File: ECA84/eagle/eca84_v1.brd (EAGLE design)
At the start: 223 x 127 mm, 34 parts

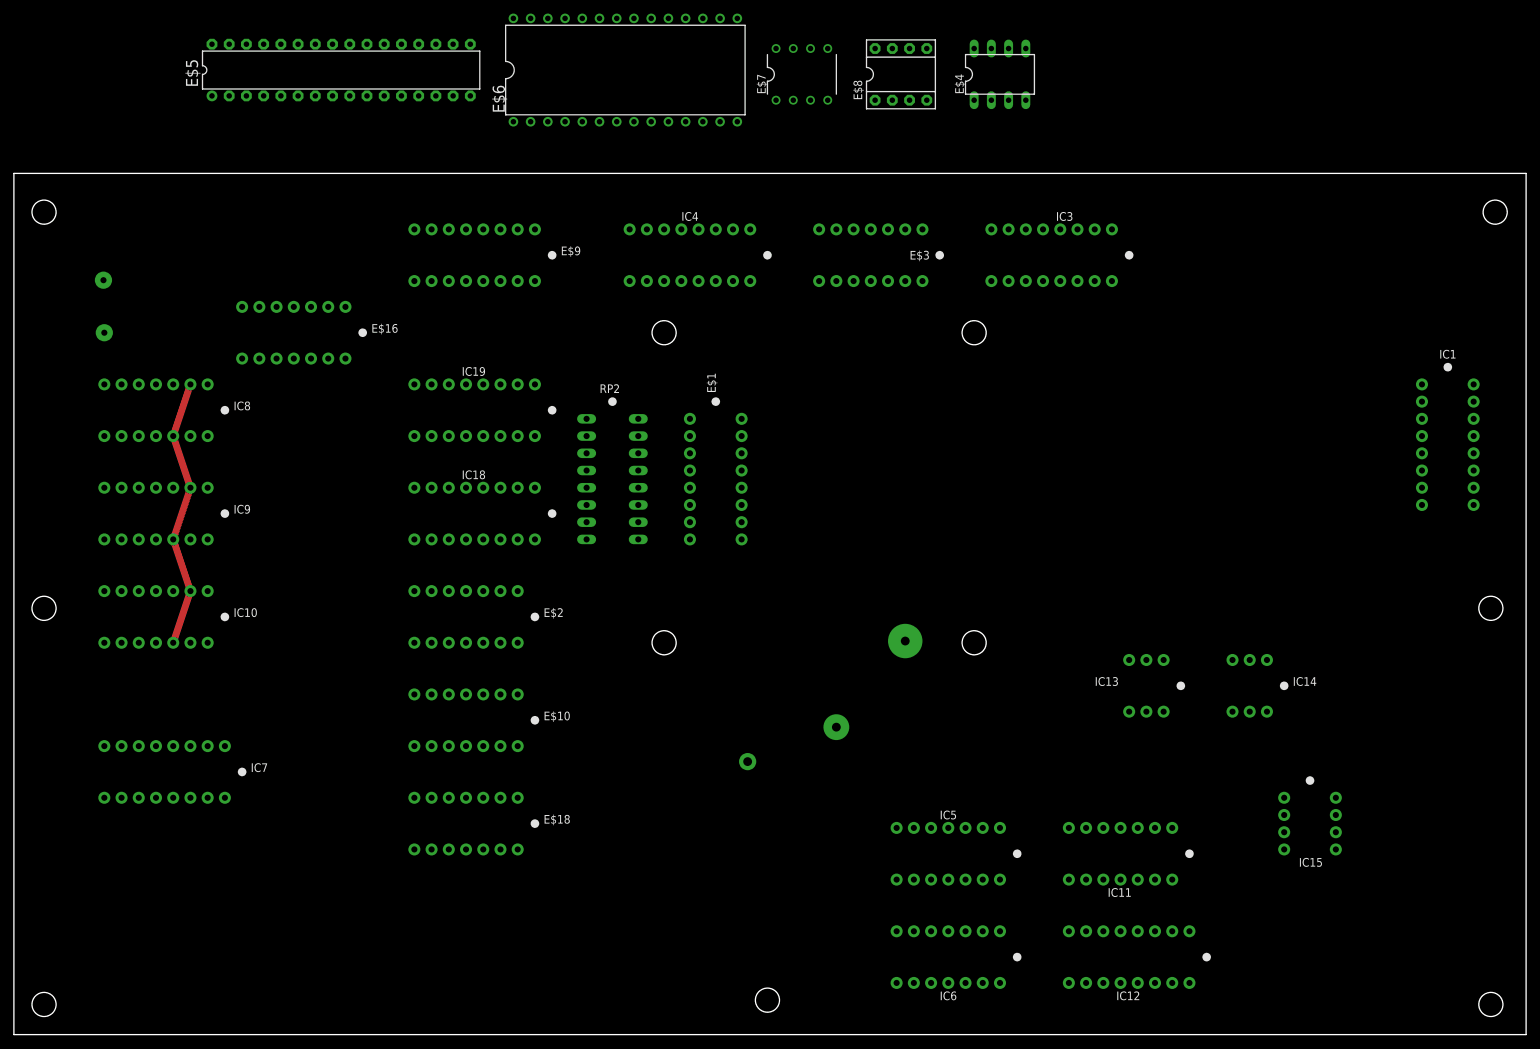
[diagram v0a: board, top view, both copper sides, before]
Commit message: trazado top, agr poligono vcc
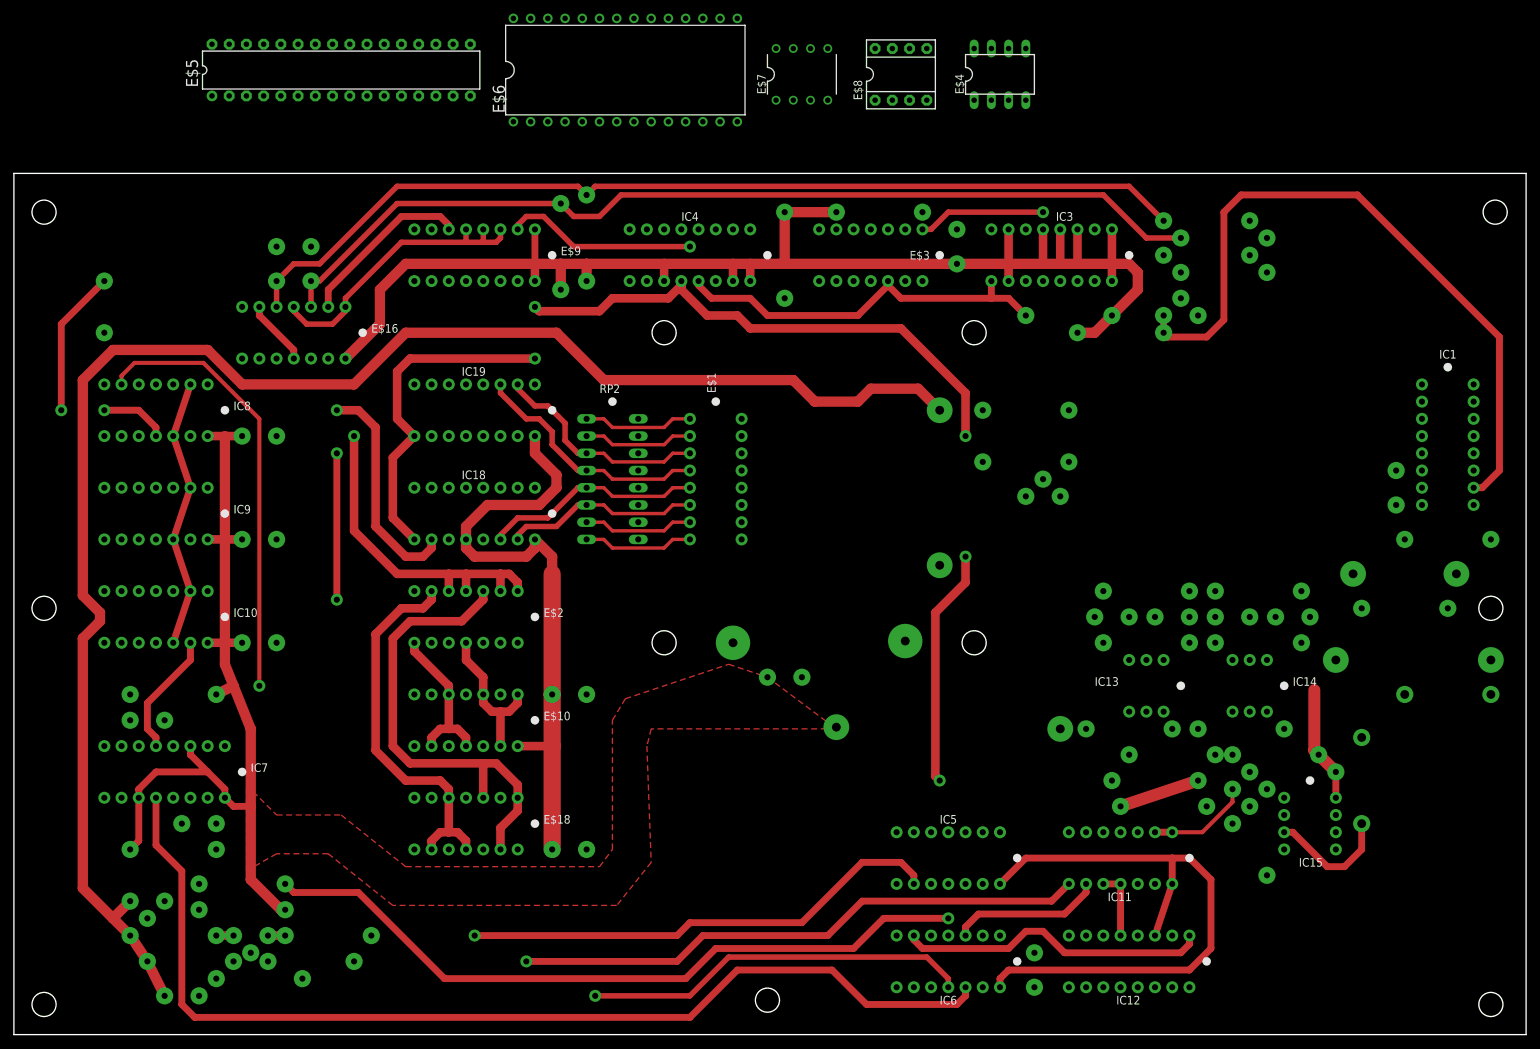
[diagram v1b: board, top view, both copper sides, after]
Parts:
- removed E$13: (no value), eca84:ROUND-4
- added E$100, E$101, E$102, E$103, E$104, E$105, E$106, E$107, E$108, E$109, E$110, E$111, E$112, E$113, E$114, E$115, E$116, E$117, E$118, E$119, E$120, E$121, E$122, E$123, E$124, E$125, E$126, E$127, E$128, E$129, E$130, E$131, E$132, E$133, E$134, E$135, E$136, E$137, E$138, E$139, E$140, E$141, E$142, E$143, E$147, E$148, E$152, E$153, E$154, E$168, E$20, E$21, E$22, E$23, E$24, E$25, E$26, E$27, E$28, E$29, E$30, E$31, E$32, E$33, E$34, E$35, E$36, E$37, E$38, E$39, E$40, E$41, E$42, E$43, E$44, E$45, E$46, E$47, E$48, E$49, E$50, E$51, E$52, E$53, E$54, E$55, E$62, E$63, E$64, E$65, E$66, E$67, E$68, E$69, E$70, E$71, E$72, E$73, E$74, E$75, E$76, E$77, E$78, E$79, E$80, E$81, E$82, E$83, E$84, E$85, E$86, E$87, E$88, E$89, E$90, E$91, E$92, E$93, E$94, E$95, E$96: (no value), eca84:ROUND-3
- added E$144, E$159, E$160, E$161, E$162, E$163, E$166: (no value), eca84:ROUND-5
- added E$145, E$146, E$149, E$150, E$151, E$164, E$165, E$17, E$19, E$56, E$57, E$58, E$59, E$60, E$61, E$97, E$98, E$99: (no value), eca84:ROUND-1
- added E$155, E$156, E$157, E$158: (no value), eca84:ROUND-4
- added E$167: (no value), eca84:ROUND-6
- moved IC11 0.64 mm to (163.2, 26.0)
- moved IC5 0.64 mm to (137.8, 26.0)
- moved IC12 0.63 mm to (164.5, 10.8)
- moved IC6 0.63 mm to (137.8, 10.8)
- moved E$11 0.18 mm to (13.3, 111.1)
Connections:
- new net S$10: IC6.P$12, IC7.P$12
- new net S$11: E$42.P$1, E$43.P$1
- new net S$12: E$47.P$1, E$48.P$1
- new net S$13: E$144.P$1, E$34.P$1, E$37.P$1, E$38.P$1, E$39.P$1
- new net S$14: E$56.P$1, E$57.P$1
- new net S$15: E$16.P$5, E$62.P$1, E$67.P$1, E$72.P$1
- new net S$16: E$16.P$3, E$63.P$1, E$66.P$1, E$73.P$1
- new net S$17: E$16.P$2, E$9.P$6
- new net S$18: E$16.P$1, E$16.P$4, E$9.P$3, E$9.P$4, E$9.P$5
- new net S$19: E$149.P$1, E$9.P$2
- new net S$2: E$11.P$1, E$19.P$1
- new net S$20: E$16.P$14, E$68.P$1, E$69.P$1, E$80.P$1, E$81.P$1, E$83.P$1, E$9.P$1, E$9.P$16, E$95.P$1, E$96.P$1, IC3.P$1, IC3.P$10, IC3.P$16, IC3.P$3, IC3.P$4, IC3.P$5, IC3.P$7, IC4.P$11, IC4.P$15, IC4.P$16
- new net S$21: E$150.P$1, E$61.P$1, IC4.P$12
- new net S$22: E$2.P$1, E$2.P$2, E$2.P$4, E$2.P$5, E$59.P$1
- new net S$23: E$3.P$12, E$82.P$1, IC3.P$9, IC4.P$13
- new net S$24: E$58.P$1, IC18.P$10
- new net S$25: E$60.P$1, IC18.P$9, IC19.P$9
- new net S$26: E$1.P$3, IC19.P$2, RP2.P$3
- new net S$27: E$1.P$4, IC19.P$3, RP2.P$4
- new net S$28: E$1.P$6, IC18.P$15, RP2.P$6
- new net S$29: E$1.P$7, RP2.P$7
- new net S$3: E$17.P$1, IC8.P$11
- new net S$30: E$10.P$14, E$91.P$1, E$93.P$1, IC18.P$12, IC18.P$16, IC19.P$16
- new net S$31: E$1.P$1, RP2.P$1
- new net S$32: E$1.P$2, RP2.P$2
- new net S$33: E$1.P$5, IC18.P$14, RP2.P$5
- new net S$34: E$1.P$8, RP2.P$8
- new net S$35: E$98.P$1, IC11.P$8
- new net S$36: E$10.P$1, E$10.P$13, E$10.P$3, E$2.P$11
- new net S$37: E$10.P$11, E$10.P$5, E$10.P$9, E$2.P$8
- new net S$38: E$18.P$11, E$18.P$5, E$18.P$9, E$2.P$6
- new net S$39: IC11.P$9, IC6.P$3
- new net S$4: E$16.P$11, E$16.P$6
- new net S$40: E$18.P$1, E$18.P$13, E$18.P$3, E$2.P$3
- new net S$41: E$97.P$1, IC5.P$9
- new net S$42: E$151.P$1, E$3.P$1
- new net S$43: E$78.P$1, E$79.P$1, IC1.P$10
- new net S$44: IC12.P$1, IC6.P$6
- new net S$45: IC11.P$14, IC12.P$3, IC5.P$14, IC6.P$14
- new net S$46: IC11.P$10, IC11.P$11, IC12.P$5
- new net S$47: E$155.P$1, IC15.P$3
- new net S$48: E$152.P$1, E$153.P$1, IC15.P$8
- new net S$49: E$106.P$1, IC11.P$1, IC11.P$2
- new net S$5: E$145.P$1, IC8.P$6
- new net S$50: E$109.P$1, E$110.P$1
- new net S$51: E$164.P$1, E$165.P$1
- new net S$6: IC10.P$13, IC7.P$5
- new net S$7: E$146.P$1, E$55.P$1
- new net S$9: E$99.P$1, IC6.P$11
- new net VCC: E$20.P$1, E$22.P$1, E$24.P$1, E$29.P$1, E$33.P$1, E$54.P$1, IC10.P$14, IC7.P$11, IC7.P$16, IC7.P$3, IC8.P$14, IC9.P$14
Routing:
- net S$13: track 0.00 -> 240.5 mm
- net S$20: track 0.00 -> 207.5 mm
- net S$10: track 0.00 -> 155.2 mm
- net S$15: track 0.00 -> 143.6 mm
- net S$16: track 0.00 -> 141.5 mm
- net VCC: track 0.00 -> 125.8 mm
- net S$7: track 0.00 -> 107.3 mm
- net S$43: track 0.00 -> 103.5 mm
- net S$30: track 0.00 -> 92.1 mm
- net S$45: track 0.00 -> 90.2 mm
- net S$35: track 0.00 -> 84.7 mm
- net S$21: track 0.00 -> 79.3 mm
- net S$41: track 0.00 -> 71.3 mm
- net S$40: track 0.00 -> 69.3 mm
- net S$5: track 0.00 -> 65.2 mm
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- added copper zone on layer 1, net VCC

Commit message: poligono top casi terminado
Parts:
- moved E$14 0.25 mm to (121.3, 45.1)
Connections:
- removed net S$30: E$10.P$14, E$91.P$1, E$93.P$1, IC18.P$12, IC18.P$16, IC19.P$16
- removed net S$48: E$152.P$1, E$153.P$1, IC15.P$8
- net VCC: now also E$10.P$14, E$100.P$1, E$14.P$1, E$152.P$1, E$153.P$1, E$167.P$1, E$2.P$14, E$91.P$1, E$93.P$1, IC15.P$8, IC18.P$12, IC18.P$16, IC19.P$16, RP2.P$16
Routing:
- net VCC: track 125.8 -> 257.5 mm
- net S$30: track 92.1 -> 0.00 mm
- net S$48: track 17.2 -> 0.00 mm
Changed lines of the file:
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@@
 </element>
 <element name="E$12" library="eca84" package="ROUND-3" value="" x="13.335" y="103.505" smashed="yes"/>
-<element name="E$14" library="eca84" package="ROUND-5" value="" x="121.285" y="45.339" smashed="yes"/>
+<element name="E$14" library="eca84" package="ROUND-5" value="" x="121.285" y="45.085" smashed="yes"/>
 <element name="E$15" library="eca84" package="ROUND-6" value="" x="131.445" y="58.039" smashed="yes"/>
 <element name="IC7" library="eca84" package="DIL-16" value="" x="22.225" y="38.735" smashed="yes">
@@
 <wire x1="34.925" y1="33.655" x2="32.385" y2="33.655" width="1.016" layer="1"/>
 <wire x1="31.115" y1="34.925" x2="32.385" y2="33.655" width="1.016" layer="1"/>
-<polygon width="0" layer="1">
-<vertex x="34.29" y="36.83"/>
-<vertex x="38.735" y="32.385"/>
+<polygon width="0.1524" layer="1" thermals="no">
+<vertex x="34.925" y="35.56"/>
+<vertex x="38.1" y="32.385"/>
 <vertex x="48.26" y="32.385"/>
 <vertex x="57.785" y="24.765"/>
 <vertex x="86.36" y="24.765"/>
-<vertex x="88.265" y="27.305"/>
-<vertex x="88.265" y="46.355"/>
-<vertex x="90.17" y="49.53"/>
-<vertex x="105.41" y="54.61"/>
-<vertex x="111.125" y="52.705"/>
+<vertex x="88.9" y="28.151665625"/>
+<vertex x="88.9" y="47.625"/>
+<vertex x="90.805" y="49.53"/>
+<vertex x="108.585" y="57.15"/>
+<vertex x="111.76" y="53.34"/>
 <vertex x="121.285" y="45.085"/>
-<vertex x="93.98" y="45.085"/>
-<vertex x="93.345" y="42.545"/>
-<vertex x="93.98" y="25.4"/>
+<vertex x="95.885" y="45.085"/>
+<vertex x="93.957321875" y="43.157321875"/>
+<vertex x="94.586903125" y="26.158628125"/>
 <vertex x="88.9" y="19.05"/>
 <vertex x="55.88" y="19.05"/>
 <vertex x="46.355" y="26.67"/>
-<vertex x="38.735" y="26.67"/>
-<vertex x="34.29" y="24.13"/>
+<vertex x="38.1" y="26.67"/>
+<vertex x="34.925" y="23.495"/>
 </polygon>
+<polygon width="0.1524" layer="1" thermals="no">
+<vertex x="101.6" y="94.615"/>
+<vertex x="104.14" y="94.615"/>
+<vertex x="105.41" y="93.345"/>
+<vertex x="105.41" y="69.215"/>
+<vertex x="109.22" y="65.405"/>
+<vertex x="128.905" y="65.405"/>
+<vertex x="130.175" y="66.675"/>
+<vertex x="130.175" y="73.025"/>
+<vertex x="131.445" y="74.295"/>
+<vertex x="146.05" y="83.82"/>
+<vertex x="147.955" y="97.155"/>
+<vertex x="154.305" y="103.505"/>
+<vertex x="155.575" y="103.505"/>
+<vertex x="156.845" y="102.235"/>
+<vertex x="156.845" y="100.965"/>
+<vertex x="151.765" y="95.885"/>
+<vertex x="149.225" y="82.55"/>
+<vertex x="147.955" y="81.28"/>
+<vertex x="146.05" y="80.01"/>
+<vertex x="146.05" y="74.93"/>
+<vertex x="151.13" y="67.31"/>
+<vertex x="151.13" y="59.055"/>
+<vertex x="156.845" y="53.34"/>
+<vertex x="189.23" y="53.34"/>
+<vertex x="195.58" y="52.07"/>
+<vertex x="203.835" y="55.88"/>
+<vertex x="203.835" y="66.675"/>
+<vertex x="212.725" y="77.47"/>
+<vertex x="217.17" y="74.295"/>
+<vertex x="217.17" y="73.025"/>
+<vertex x="212.725" y="73.025"/>
+<vertex x="207.01" y="66.04"/>
+<vertex x="207.01" y="55.245"/>
+<vertex x="205.74" y="53.975"/>
+<vertex x="195.58" y="49.53"/>
+<vertex x="191.135" y="44.45"/>
+<vertex x="189.23" y="50.165"/>
+<vertex x="151.13" y="49.53"/>
+<vertex x="151.13" y="29.845"/>
+<vertex x="154.94" y="26.035"/>
+<vertex x="147.955" y="25.4"/>
+<vertex x="147.955" y="66.04"/>
+<vertex x="142.875" y="73.66"/>
+<vertex x="136.525" y="73.66"/>
+<vertex x="133.35" y="71.755"/>
+<vertex x="133.35" y="64.77"/>
+<vertex x="130.175" y="61.595"/>
+<vertex x="109.855" y="61.595"/>
+<vertex x="104.14" y="56.515"/>
+<vertex x="100.965" y="64.135"/>
+<vertex x="78.74" y="64.135"/>
+<vertex x="78.74" y="66.675"/>
+<vertex x="74.295" y="71.12"/>
+<vertex x="79.375" y="71.12"/>
+<vertex x="80.645" y="69.85"/>
+<vertex x="101.6" y="69.85"/>
+</polygon>
+<contactref element="E$100" pad="P$1"/>
+<contactref element="E$14" pad="P$1"/>
+<wire x1="121.285" y1="45.085" x2="116.205" y2="46.99" width="2.54" layer="1"/>
+<contactref element="E$167" pad="P$1"/>
+<wire x1="106.045" y1="57.785" x2="106.045" y2="53.34" width="2.54" layer="1"/>
+<contactref element="IC19" pad="P$16"/>
+<wire x1="76.835" y1="85.725" x2="76.835" y2="88.265" width="1.524" layer="1"/>
+<wire x1="80.01" y1="82.55" x2="76.835" y2="85.725" width="1.524" layer="1"/>
+<wire x1="80.01" y1="80.645" x2="80.01" y2="82.55" width="1.524" layer="1"/>
+<wire x1="77.47" y1="78.105" x2="80.01" y2="80.645" width="1.524" layer="1"/>
+<wire x1="69.85" y1="78.105" x2="77.47" y2="78.105" width="1.524" layer="1"/>
+<wire x1="66.675" y1="74.93" x2="69.85" y2="78.105" width="1.524" layer="1"/>
+<contactref element="IC18" pad="P$12"/>
+<wire x1="66.675" y1="73.025" x2="66.675" y2="74.93" width="1.524" layer="1"/>
+<wire x1="66.675" y1="73.025" x2="66.675" y2="71.755" width="1.524" layer="1"/>
+<wire x1="66.675" y1="71.755" x2="67.945" y2="70.485" width="1.524" layer="1"/>
+<wire x1="67.945" y1="70.485" x2="76.835" y2="70.485" width="1.524" layer="1"/>
+<contactref element="IC18" pad="P$16"/>
+<wire x1="76.835" y1="70.485" x2="76.835" y2="73.025" width="1.524" layer="1"/>
+<contactref element="E$10" pad="P$14"/>
+<contactref element="E$93" pad="P$1"/>
+<wire x1="79.375" y1="50.165" x2="79.375" y2="57.785" width="2.54" layer="1"/>
+<wire x1="79.375" y1="57.785" x2="79.375" y2="67.945" width="2.54" layer="1"/>
+<wire x1="79.375" y1="42.545" x2="79.375" y2="50.165" width="2.54" layer="1"/>
+<wire x1="74.295" y1="42.545" x2="79.375" y2="42.545" width="1.27" layer="1"/>
+<contactref element="E$91" pad="P$1"/>
+<wire x1="79.375" y1="27.305" x2="79.375" y2="42.545" width="2.54" layer="1"/>
+<contactref element="E$2" pad="P$14"/>
+<wire x1="74.295" y1="57.785" x2="79.375" y2="57.785" width="1.27" layer="1"/>
+<contactref element="RP2" pad="P$16"/>
+<wire x1="92.075" y1="90.805" x2="95.25" y2="93.98" width="1.27" layer="1"/>
+<wire x1="95.25" y1="93.98" x2="103.505" y2="93.98" width="1.27" layer="1"/>
+<contactref element="IC15" pad="P$8"/>
+<contactref element="E$153" pad="P$1"/>
+<wire x1="194.945" y1="34.925" x2="194.945" y2="38.735" width="1.016" layer="1"/>
+<contactref element="E$152" pad="P$1"/>
+<wire x1="194.945" y1="38.735" x2="192.405" y2="41.275" width="1.778" layer="1"/>
+<wire x1="192.405" y1="41.275" x2="191.77" y2="41.91" width="1.778" layer="1"/>
+<wire x1="191.77" y1="41.91" x2="191.77" y2="50.8" width="1.778" layer="1"/>
 </signal>
 <signal name="S$10">
@@
 <wire x1="97.155" y1="78.105" x2="99.695" y2="78.105" width="0.508" layer="1"/>
 </signal>
-<signal name="S$30">
-<contactref element="IC19" pad="P$16"/>
-<wire x1="76.835" y1="85.725" x2="76.835" y2="88.265" width="1.524" layer="1"/>
-<wire x1="80.01" y1="82.55" x2="76.835" y2="85.725" width="1.524" layer="1"/>
-<wire x1="80.01" y1="80.645" x2="80.01" y2="82.55" width="1.524" layer="1"/>
-<wire x1="77.47" y1="78.105" x2="80.01" y2="80.645" width="1.524" layer="1"/>
-<wire x1="69.85" y1="78.105" x2="77.47" y2="78.105" width="1.524" layer="1"/>
-<contactref element="IC18" pad="P$16"/>
-<wire x1="66.675" y1="74.93" x2="69.85" y2="78.105" width="1.524" layer="1"/>
-<contactref element="IC18" pad="P$12"/>
-<wire x1="66.675" y1="73.025" x2="66.675" y2="74.93" width="1.524" layer="1"/>
-<wire x1="76.835" y1="71.755" x2="76.835" y2="73.025" width="1.524" layer="1"/>
-<wire x1="75.565" y1="70.485" x2="76.835" y2="71.755" width="1.524" layer="1"/>
-<wire x1="66.675" y1="73.025" x2="66.675" y2="71.755" width="1.524" layer="1"/>
-<wire x1="66.675" y1="71.755" x2="67.945" y2="70.485" width="1.524" layer="1"/>
-<wire x1="67.945" y1="70.485" x2="75.565" y2="70.485" width="1.524" layer="1"/>
-<contactref element="E$91" pad="P$1"/>
-<contactref element="E$93" pad="P$1"/>
-<wire x1="79.375" y1="27.305" x2="79.375" y2="42.545" width="2.54" layer="1"/>
-<wire x1="79.375" y1="42.545" x2="79.375" y2="50.165" width="2.54" layer="1"/>
-<wire x1="79.375" y1="50.165" x2="79.375" y2="67.945" width="2.54" layer="1"/>
-<wire x1="76.835" y1="73.025" x2="79.375" y2="70.485" width="1.524" layer="1"/>
-<wire x1="79.375" y1="70.485" x2="79.375" y2="67.945" width="1.524" layer="1"/>
-<contactref element="E$10" pad="P$14"/>
-<wire x1="74.295" y1="42.545" x2="79.375" y2="42.545" width="1.27" layer="1"/>
-</signal>
 <signal name="S$31">
 <contactref element="RP2" pad="P$1"/>
@@
 <wire x1="188.595" y1="29.845" x2="187.325" y2="29.845" width="1.016" layer="1"/>
 </signal>
-<signal name="S$48">
-<contactref element="IC15" pad="P$8"/>
-<contactref element="E$153" pad="P$1"/>
-<wire x1="194.945" y1="34.925" x2="194.945" y2="38.735" width="1.016" layer="1"/>
-<contactref element="E$152" pad="P$1"/>
-<wire x1="194.945" y1="38.735" x2="192.405" y2="41.275" width="1.778" layer="1"/>
-<wire x1="192.405" y1="41.275" x2="191.77" y2="41.91" width="1.778" layer="1"/>
-<wire x1="191.77" y1="41.91" x2="191.77" y2="50.8" width="1.778" layer="1"/>
-</signal>
 <signal name="S$49">

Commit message: iniciando pistas bottom
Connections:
- removed net S$1: IC10.P$12, IC10.P$2, IC8.P$12, IC8.P$2, IC9.P$12, IC9.P$2
- removed net S$14: E$56.P$1, E$57.P$1
- removed net S$19: E$149.P$1, E$9.P$2
- removed net S$20: E$16.P$14, E$68.P$1, E$69.P$1, E$80.P$1, E$81.P$1, E$83.P$1, E$9.P$1, E$9.P$16, E$95.P$1, E$96.P$1, IC3.P$1, IC3.P$10, IC3.P$16, IC3.P$3, IC3.P$4, IC3.P$5, IC3.P$7, IC4.P$11, IC4.P$15, IC4.P$16
- removed net S$21: E$150.P$1, E$61.P$1, IC4.P$12
- removed net S$25: E$60.P$1, IC18.P$9, IC19.P$9
- removed net S$3: E$17.P$1, IC8.P$11
- removed net S$36: E$10.P$1, E$10.P$13, E$10.P$3, E$2.P$11
- removed net S$41: E$97.P$1, IC5.P$9
- new net S$30: IC8.P$13, IC9.P$6
- new net S$48: IC9.P$1, IC9.P$8
- new net S$52: IC10.P$6, IC9.P$13
- new net S$53: IC10.P$1, IC10.P$8
- new net S$54: E$27.P$1, E$28.P$1, IC7.P$7
- new net S$55: E$26.P$1, IC7.P$6
- new net S$56: IC7.P$13, IC7.P$9
- new net S$57: IC7.P$1, IC7.P$8
- new net S$58: E$30.P$1, IC7.P$14
- new net S$59: E$31.P$1, E$32.P$1, IC7.P$15
- new net S$60: E$35.P$1, E$53.P$1
- new net S$61: E$44.P$1, E$45.P$1, E$46.P$1
- new net S$62: E$40.P$1, E$41.P$1
- new net S$63: E$12.P$1, E$21.P$1, E$23.P$1, E$25.P$1, E$50.P$1, E$51.P$1, IC8.P$7
- new net S$64: E$16.P$7, E$3.P$7, E$64.P$1, E$65.P$1, E$71.P$1, E$9.P$8, IC3.P$6, IC3.P$8, IC4.P$8
- new net S$65: E$149.P$1, E$150.P$1, E$3.P$2, E$60.P$1, E$61.P$1, E$70.P$1, E$9.P$2, IC18.P$9, IC19.P$9, IC3.P$2, IC4.P$12
- new net S$66: E$3.P$9, IC4.P$10
- new net S$67: E$168.P$1, E$3.P$8
- new net S$68: E$16.P$13, E$9.P$15
- new net S$69: E$16.P$10, E$56.P$1, E$57.P$1, E$9.P$10, E$9.P$7
- new net S$8: IC8.P$1, IC8.P$8
- net S$11: now also E$36.P$1
- net S$12: now also E$49.P$1
- net S$2: now also E$17.P$1, IC8.P$11
- net S$22: now also E$10.P$1, E$10.P$13, E$10.P$3, E$2.P$10, E$2.P$11, E$2.P$12, E$2.P$13, E$2.P$9, IC19.P$6
- net S$24: now also E$16.P$12, E$9.P$9
- net S$35: now also IC10.P$12, IC10.P$2, IC8.P$12, IC8.P$2, IC9.P$12, IC9.P$2
- net S$5: now also E$97.P$1, IC5.P$9
- net S$7: now also E$52.P$1
- net S$9: now also IC7.P$2
- net VCC: now also E$138.P$1, E$16.P$14, E$68.P$1, E$69.P$1, E$80.P$1, E$81.P$1, E$83.P$1, E$9.P$1, E$9.P$16, E$95.P$1, E$96.P$1, IC1.P$16, IC3.P$1, IC3.P$10, IC3.P$16, IC3.P$3, IC3.P$4, IC3.P$5, IC3.P$7, IC4.P$11, IC4.P$15, IC4.P$16
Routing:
- net VCC: track 257.5 -> 492.0 mm
- net S$20: track 207.5 -> 0.00 mm
- net S$65: track 0.00 -> 157.2 mm
- net S$21: track 79.3 -> 0.00 mm
- net S$5: track 65.2 -> 136.5 mm
- net S$41: track 71.3 -> 0.00 mm
- net S$25: track 49.6 -> 0.00 mm
- net S$35: track 84.7 -> 124.9 mm
- net S$1: track 40.2 -> 0.00 mm
- net S$19: track 28.4 -> 0.00 mm
- net S$22: track 50.1 -> 72.6 mm
- net S$36: track 22.4 -> 0.00 mm
- net S$69: track 0.00 -> 21.6 mm
- net S$14: track 21.6 -> 0.00 mm
- net S$57: track 0.00 -> 21.4 mm
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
